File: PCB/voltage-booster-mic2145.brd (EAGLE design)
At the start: 17.8 x 20.3 mm, 20 parts

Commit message: Ad/update component values.
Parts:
- C1: value (none) -> 10uF/6.3V
- C4: value 10uF -> 10uF/16V
- R2: value 200 -> 470
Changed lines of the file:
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@@
 <attribute name="VALUE" x="4.064" y="7.493" size="0.4064" layer="27" font="vector" align="center"/>
 </element>
-<element name="C1" library="rlc" library_urn="urn:adsk.eagle:library:4192893" package="0603-CAP" package3d_urn="urn:adsk.eagle:package:4193021/2" value="" x="9.906" y="12.954" smashed="yes" rot="R180">
+<element name="C1" library="rlc" library_urn="urn:adsk.eagle:library:4192893" package="0603-CAP" package3d_urn="urn:adsk.eagle:package:4193021/2" value="10uF/6.3V" x="9.906" y="12.954" smashed="yes" rot="R180">
 <attribute name="COST01" value="0.12" x="-6.604" y="30.734" size="1.778" layer="27" rot="R180" display="off"/>
 <attribute name="COST10" value="0.09" x="-6.604" y="30.734" size="1.778" layer="27" rot="R180" display="off"/>
@@
 <attribute name="VALUE" x="2.54" y="5.334" size="0.2" layer="27" align="center"/>
 </element>
-<element name="R2" library="rlc" library_urn="urn:adsk.eagle:library:4192893" package="0603-RES" package3d_urn="urn:adsk.eagle:package:4193040/2" value="200" x="2.54" y="6.858" smashed="yes" rot="R180">
+<element name="R2" library="rlc" library_urn="urn:adsk.eagle:library:4192893" package="0603-RES" package3d_urn="urn:adsk.eagle:package:4193040/2" value="470" x="2.54" y="6.858" smashed="yes" rot="R180">
 <attribute name="COST01" value="0.10" x="2.54" y="6.858" size="1.778" layer="27" rot="R180" display="off"/>
 <attribute name="COST10" value="0.05" x="2.54" y="6.858" size="1.778" layer="27" rot="R180" display="off"/>
@@
 <attribute name="VALUE" x="9.906" y="8.89" size="0.2" layer="27" align="center"/>
 </element>
-<element name="C4" library="rlc" library_urn="urn:adsk.eagle:library:4192893" package="0603-CAP" package3d_urn="urn:adsk.eagle:package:4193021/2" value="10uF" x="14.478" y="4.953" smashed="yes">
+<element name="C4" library="rlc" library_urn="urn:adsk.eagle:library:4192893" package="0603-CAP" package3d_urn="urn:adsk.eagle:package:4193021/2" value="10uF/16V" x="14.478" y="4.953" smashed="yes">
 <attribute name="COST01" value="0.12" x="14.478" y="4.953" size="1.778" layer="27" display="off"/>
 <attribute name="COST10" value="0.09" x="14.478" y="4.953" size="1.778" layer="27" display="off"/>

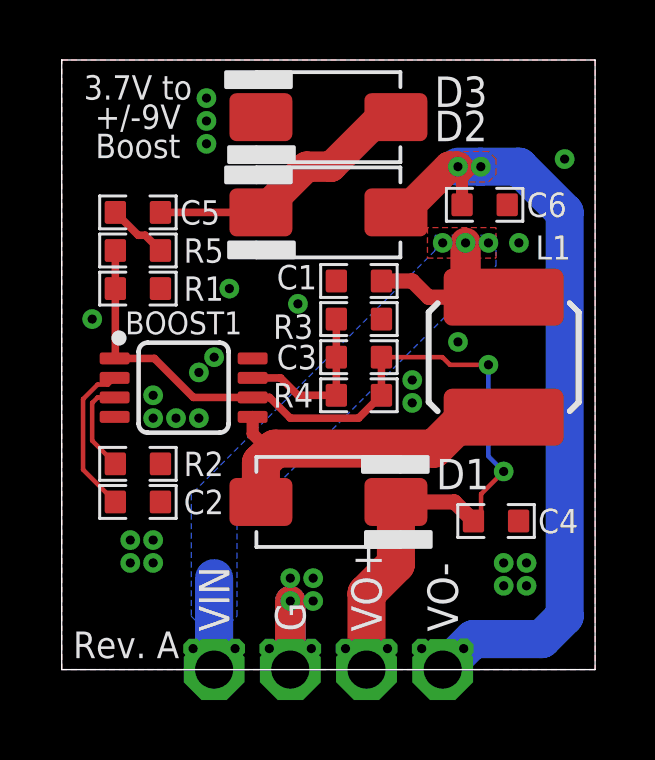
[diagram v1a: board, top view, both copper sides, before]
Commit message: Fix error where neg-volt section on wrong signal.
Bumped rev to B
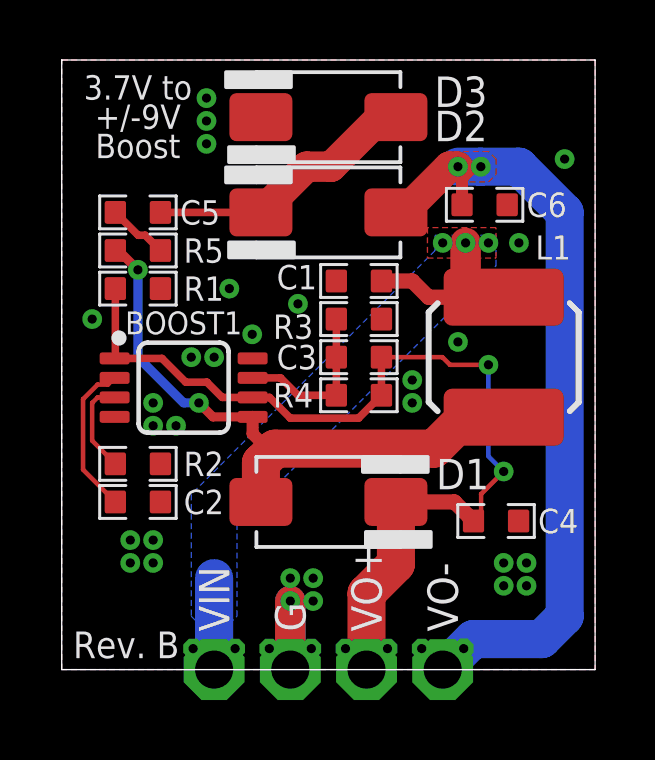
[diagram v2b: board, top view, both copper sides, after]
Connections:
- net SW: now also R5.1
- net VOUT: no longer R5.1
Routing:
- net SW: track 11.5 -> 20.0 mm, vias 0 -> 2
- net VOUT: track 33.3 -> 32.0 mm
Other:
- board text added: "Rev. B"
- board text removed: "Rev. A"
